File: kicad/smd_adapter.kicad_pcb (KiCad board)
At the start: 2 copper layers, 65.2 x 74.4 mm, 254 parts, among them J1 Conn_01x01_Pin, J10 Conn_01x01_Pin, J11 Conn_01x01_Pin, J12 Conn_01x01_Pin, J13 Conn_01x01_Pin, J14 Conn_01x01_Pin, J15 Conn_01x01_Pin, J16 Conn_01x01_Pin, J17 Conn_01x01_Pin, J18 Conn_01x01_Pin, J19 Conn_01x01_Pin, J2 Conn_01x01_Pin, J20 Conn_01x01_Pin, J21 Conn_01x01_Pin, J22 Conn_01x01_Pin, J23 Conn_01x01_Pin, J24 Conn_01x01_Pin, J25 Conn_01x01_Pin, J26 Conn_01x01_Pin, J27 Conn_01x01_Pin, J28 Conn_01x01_Pin, J29 Conn_01x01_Pin, J3 Conn_01x01_Pin, J30 Conn_01x01_Pin, J31 Conn_01x01_Pin, J32 Conn_01x01_Pin, J33 Conn_01x01_Pin, J34 Conn_01x01_Pin, J35 Conn_01x01_Pin, J36 Conn_01x01_Pin, J37 Conn_01x01_Pin, J4 Conn_01x01_Pin, J5 Conn_01x01_Pin, J6 Conn_01x01_Pin, J7 Conn_01x01_Pin, J8 Conn_01x01_Pin, J9 Conn_01x01_Pin, U1 SOIC8, U2 SOT_32-5, U3 SOT_32-6, U5 TSSOP-10

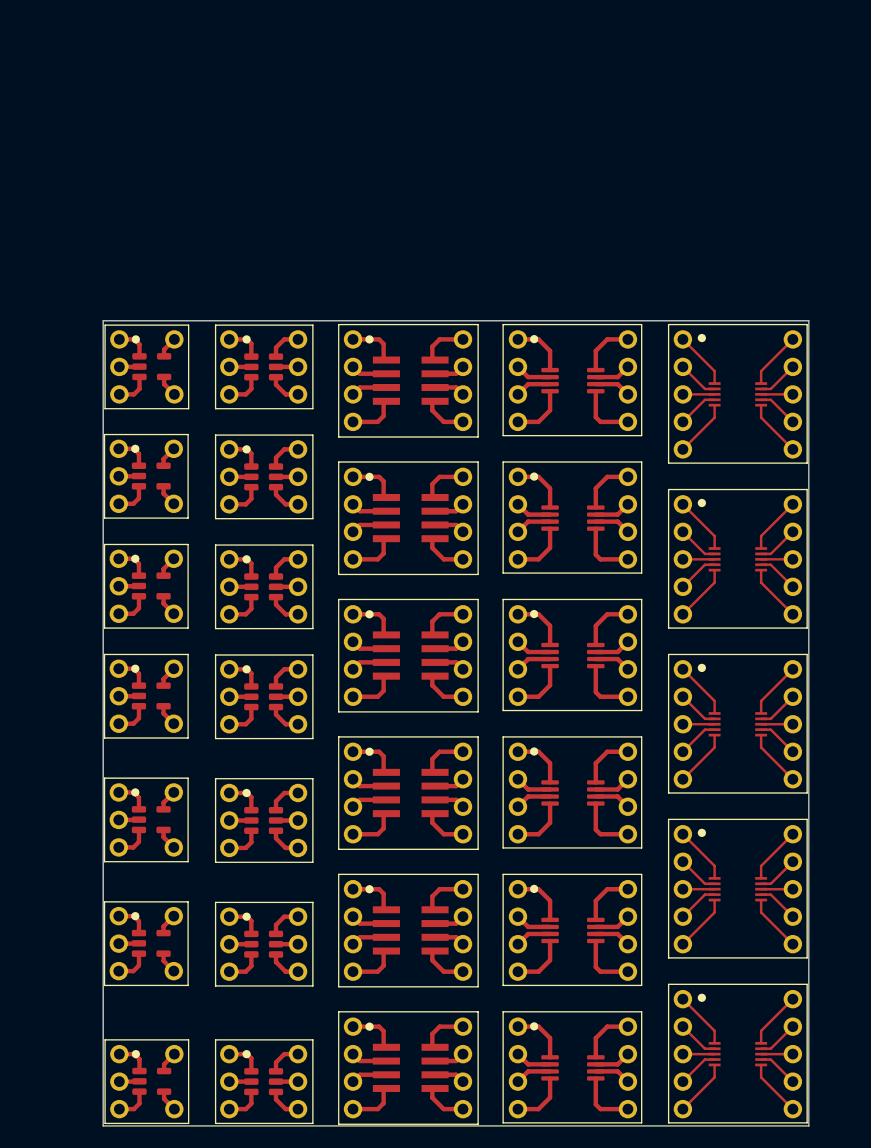
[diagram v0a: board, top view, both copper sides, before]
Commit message: Created full module footprints.
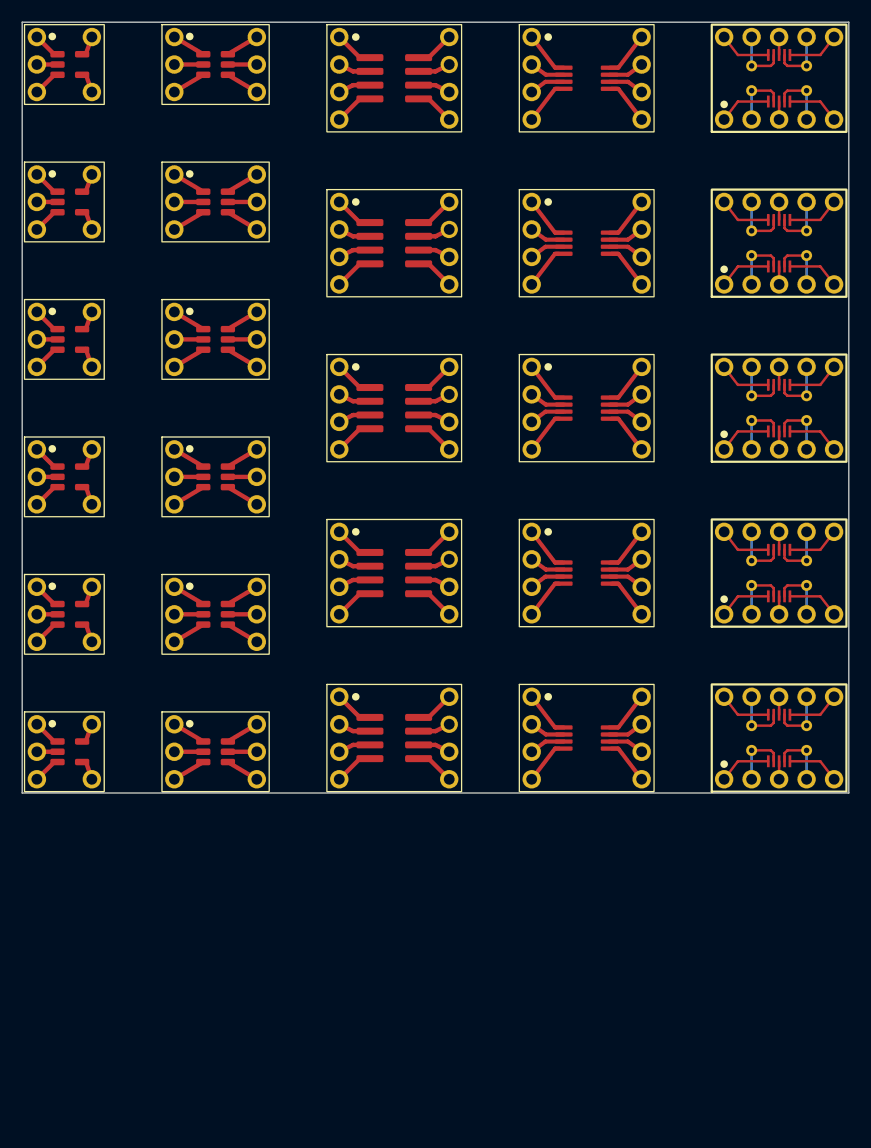
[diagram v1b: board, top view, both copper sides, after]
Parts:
- removed J1 (x7), J10 (x6), J11 (x6), J12 (x6), J13 (x6), J14 (x7), J15 (x7), J16 (x7), J17 (x7), J18 (x7), J19 (x7), J2 (x7), J20 (x6), J21 (x6), J22 (x6), J23 (x6), J24 (x6), J25 (x6), J26 (x6), J27 (x6), J28 (x5), J29 (x5), J3 (x7), J30 (x5), J31 (x5), J32 (x5), J33 (x5), J34 (x5), J35 (x5), J36 (x5), J37 (x5), J4 (x7), J5 (x7), J6 (x6), J7 (x6), J8 (x6), J9 (x6): Conn_01x01_Pin, smd_adapter:pin_pad
- removed U1 (x6): SOIC8, smd_adapter:SOIC8
- removed U2 (x7): SOT_32-5, smd_adapter:SOT-23-5
- removed U3 (x7): SOT_32-6, smd_adapter:SOT-23-6
- removed U5 (x5): TSSOP-10, smd_adapter:TSSOP-10
- removed Ue (x6): MSOP8, smd_adapter:MSOP-8
- added REF**: SMD_ADAPTER_SOT-23-5, smd_adapter:SMD_ADAPTER_SOT-23-5, F.Cu at (76.8, 40.6)
- added REF**: SMD_ADAPTER_SOT-23-6, smd_adapter:SMD_ADAPTER_SOT-23-6, F.Cu at (90.2, 66.0)
- added REF**: SMD_ADAPTER_SOT-23-6, smd_adapter:SMD_ADAPTER_SOT-23-6, F.Cu at (90.2, 40.6)
- added REF**: SMD_ADAPTER_TSSOP-10, smd_adapter:SMD_ADAPTER_TSSOP-10, F.Cu at (142.2, 59.7)
- added REF**: SMD_ADAPTER_TSSOP-10, smd_adapter:SMD_ADAPTER_TSSOP-10, F.Cu at (142.2, 90.2)
- added REF**: SMD_ADAPTER_SOIC-8, smd_adapter:SMD_ADAPTER_SOIC-8, F.Cu at (106.7, 90.2)
- added REF**: SMD_ADAPTER_SOIC-8, smd_adapter:SMD_ADAPTER_SOIC-8, F.Cu at (106.7, 74.9)
- added REF**: SMD_ADAPTER_SOT-23-5, smd_adapter:SMD_ADAPTER_SOT-23-5, F.Cu at (76.8, 27.9)
- added REF**: SMD_ADAPTER_MSOP-8, smd_adapter:SMD_ADAPTER_MSOP-8, F.Cu at (124.5, 59.7)
- added REF**: SMD_ADAPTER_SOT-23-6, smd_adapter:SMD_ADAPTER_SOT-23-6, F.Cu at (90.2, 78.7)
- added REF**: SMD_ADAPTER_MSOP-8, smd_adapter:SMD_ADAPTER_MSOP-8, F.Cu at (124.5, 29.2)
- added REF**: SMD_ADAPTER_TSSOP-10, smd_adapter:SMD_ADAPTER_TSSOP-10, F.Cu at (142.2, 74.9)
- added REF**: SMD_ADAPTER_MSOP-8, smd_adapter:SMD_ADAPTER_MSOP-8, F.Cu at (124.5, 44.5)
- added REF**: SMD_ADAPTER_SOT-23-5, smd_adapter:SMD_ADAPTER_SOT-23-5, F.Cu at (76.8, 66.0)
- added REF**: SMD_ADAPTER_SOT-23-5, smd_adapter:SMD_ADAPTER_SOT-23-5, F.Cu at (76.8, 91.4)
- added REF**: SMD_ADAPTER_SOT-23-6, smd_adapter:SMD_ADAPTER_SOT-23-6, F.Cu at (90.2, 91.4)
- added REF**: SMD_ADAPTER_TSSOP-10, smd_adapter:SMD_ADAPTER_TSSOP-10, F.Cu at (142.2, 29.2)
- added REF**: SMD_ADAPTER_SOT-23-5, smd_adapter:SMD_ADAPTER_SOT-23-5, F.Cu at (76.8, 78.7)
- added REF**: SMD_ADAPTER_MSOP-8, smd_adapter:SMD_ADAPTER_MSOP-8, F.Cu at (124.5, 90.2)
- added REF**: SMD_ADAPTER_SOT-23-6, smd_adapter:SMD_ADAPTER_SOT-23-6, F.Cu at (90.2, 53.3)
- added REF**: SMD_ADAPTER_SOIC-8, smd_adapter:SMD_ADAPTER_SOIC-8, F.Cu at (106.7, 29.2)
- added REF**: SMD_ADAPTER_TSSOP-10, smd_adapter:SMD_ADAPTER_TSSOP-10, F.Cu at (142.2, 44.5)
- added REF**: SMD_ADAPTER_MSOP-8, smd_adapter:SMD_ADAPTER_MSOP-8, F.Cu at (124.5, 74.9)
- added REF**: SMD_ADAPTER_SOT-23-6, smd_adapter:SMD_ADAPTER_SOT-23-6, F.Cu at (90.2, 27.9)
- added REF**: SMD_ADAPTER_SOT-23-5, smd_adapter:SMD_ADAPTER_SOT-23-5, F.Cu at (76.8, 53.3)
- added REF**: SMD_ADAPTER_SOIC-8, smd_adapter:SMD_ADAPTER_SOIC-8, F.Cu at (106.7, 44.5)
- added REF**: SMD_ADAPTER_SOIC-8, smd_adapter:SMD_ADAPTER_SOIC-8, F.Cu at (106.7, 59.7)
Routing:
- net Net-(J27-Pin_1): track 33.3 -> 0.00 mm
- net Net-(J24-Pin_1): track 31.1 -> 0.00 mm
- net Net-(J23-Pin_1): track 31.1 -> 0.00 mm
- net Net-(J20-Pin_1): track 31.1 -> 0.00 mm
- net Net-(J6-Pin_1): track 26.9 -> 0.00 mm
- net Net-(J9-Pin_1): track 26.5 -> 0.00 mm
- net Net-(J28-Pin_1): track 26.5 -> 0.00 mm
- net Net-(J32-Pin_1): track 26.5 -> 0.00 mm
- net Net-(J33-Pin_1): track 26.5 -> 0.00 mm
- net Net-(J37-Pin_1): track 26.5 -> 0.00 mm
- net Net-(J10-Pin_1): track 26.1 -> 0.00 mm
- net Net-(J13-Pin_1): track 24.7 -> 0.00 mm
- net Net-(J14-Pin_1): track 23.8 -> 0.00 mm
- net Net-(J16-Pin_1): track 23.3 -> 0.00 mm
- net Net-(J17-Pin_1): track 22.2 -> 0.00 mm
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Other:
- board size 65.2 x 74.4 mm -> 76.4 x 71.2 mm
- board text removed: "MSOP-8 0.65mm"
- board text removed: "SOIC-8 1.27mm"
- board text removed: "SOT23-5 0,95mm"
- board text removed: "SOT23-6 0.95mm"
- board text removed: "TSSOP-10 0.5mm"
